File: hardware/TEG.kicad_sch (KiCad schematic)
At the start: 30 parts, among them J1 TEG_IN, J2 FAN_4PIN, J3 TEST_LOAD, Q1 AO3400A, U1 BQ25504RGTT, U2 MT3608

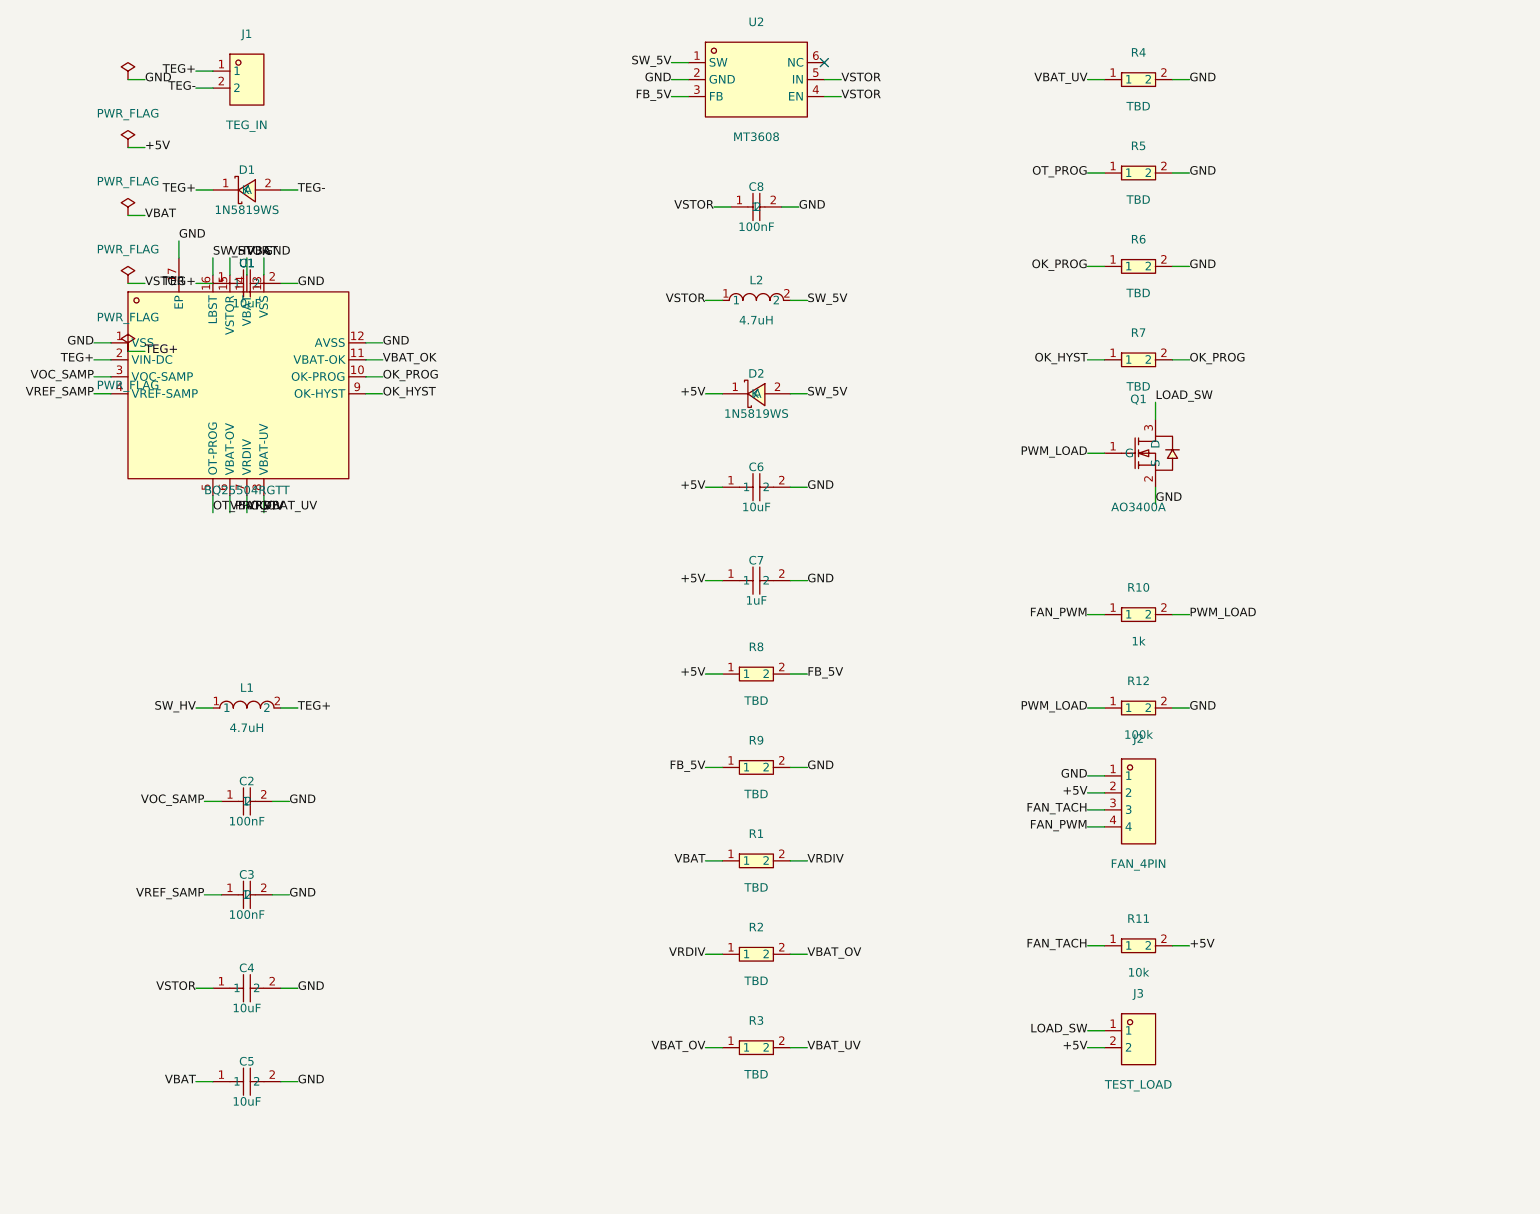
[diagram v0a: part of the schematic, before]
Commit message: Add MPPT sampling network; switch storage to supercapacitor
The BQ25504 has MPPT built in, but the draft was missing its sampling
network. Fixed:

- Add R13/R14 = 10M/10M on VOC_SAMP -> MPP ratio ~50% of Voc
  (TEG matched load; the datasheet's 78% default targets solar)
- CREF/CBYP = 10nF (C1589); drop the 100nF cap that would have slowed
  the high-impedance sampling node
- Fix OV/UV chain order to the datasheet topology and add the missing
  third OK-chain resistor (R15); set threshold values from the datasheet
  worked example (VBAT_OV 3.15V / UV 2.20V / OK 2.44V / HYST 2.80V)
- R5 = 0R ties OT_PROG to GND (65C charge cutoff)
- L1/L2 corrected to the datasheet-recommended 22uH

Storage = supercapacitor 0.22-0.47F/5.5V instead of a battery: safer in a
thermal device (no fire/cold-plating risk), simpler, matches the fan's
burst load. Trade-off noted: measure leakage vs harvest current.

32 parts / 85 pins. ERC: 1 intentional warning; board DRC: 0 violations.
BOM rev B; several high-ohm 1% resistors, the 22uH inductor and the
supercap still need JLCPCB part numbers (all extended / hand-solder).

Co-authored-by: Copilot <223556219+Copilot@users.noreply.github.com>
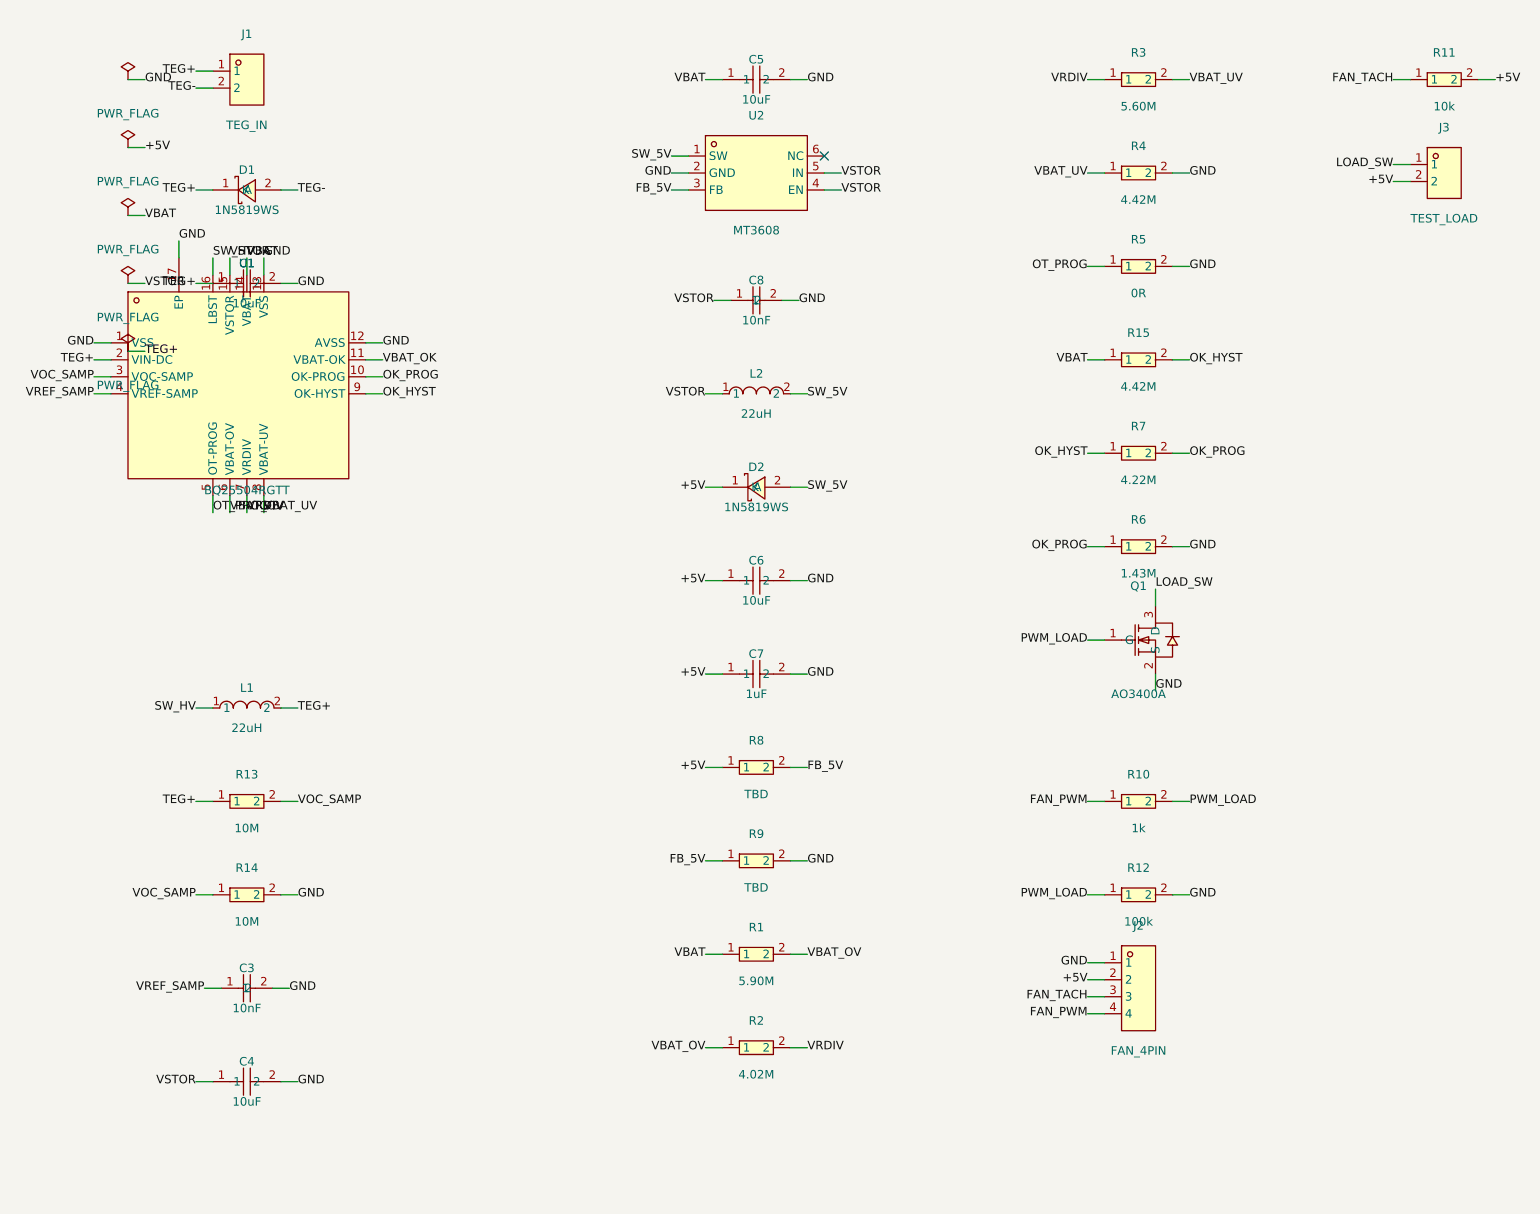
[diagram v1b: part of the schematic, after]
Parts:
- removed C2, C3, C8: 100nF, TEG:C0603, symbol TEG:CL10B104KA8NNNC
- removed R5: TBD, TEG:R0603, symbol TEG:0603WAF1003T5E
- added C3, C8: 10nF, TEG:C0603, symbol TEG:CL10B103KB8NNNC
- added R13, R14: 10M, TEG:R0603, symbol TEG:0603WAF1002T5E
- added R15: 4.42M, TEG:R0603, symbol TEG:0603WAF1003T5E
- added R5: 0R, TEG:R0603, symbol TEG:0603WAF1002T5E
- L1, L2: value 4.7uH -> 22uH; LCSC Part C5832360 -> TBD
- R1: value TBD -> 5.90M
- R2: value TBD -> 4.02M
- R3: value TBD -> 5.60M
- R4: value TBD -> 4.42M
- R6: value TBD -> 1.43M
- R7: value TBD -> 4.22M
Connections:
- net GND: now also C3.2, C8.2, R14.2, R5.2
- net OK_HYST: now also R15.2
- net OT_PROG: now also R5.1
- net TEG+: now also R13.1
- net VBAT: now also R15.1
- net VBAT_OV: now also R1.2, R2.1; no longer R2.2, R3.1
- net VOC_SAMP: now also R13.2, R14.1
- net VRDIV: now also R2.2, R3.1; no longer R1.2, R2.1
- net VREF_SAMP: now also C3.1
- net VSTOR: now also C8.1

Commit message: Set R13/R14 to a real 10M 1% part (C114606); record sourcing reality
Supercaps are not stocked by JLCPCB -> hand-solder. The odd threshold
resistors are standard E96 values but JLCPCB's public search API was
degraded and could not resolve them; note that for the buyer.

Co-authored-by: Copilot <223556219+Copilot@users.noreply.github.com>
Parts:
- R13, R14: LCSC Part TBD -> C114606
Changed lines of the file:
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@@
 		(property "Footprint" "TEG:R0603" (at 0 0 0) (effects (font (size 1.27 1.27)) hide))
 		(property "Datasheet" "~" (at 0 0 0) (effects (font (size 1.27 1.27)) hide))
-		(property "LCSC Part" "TBD" (at 0 0 0) (effects (font (size 1.27 1.27)) hide))
+		(property "LCSC Part" "C114606" (at 0 0 0) (effects (font (size 1.27 1.27)) hide))
 		(pin "2")
 		(pin "1")
@@
 		(property "Footprint" "TEG:R0603" (at 0 0 0) (effects (font (size 1.27 1.27)) hide))
 		(property "Datasheet" "~" (at 0 0 0) (effects (font (size 1.27 1.27)) hide))
-		(property "LCSC Part" "TBD" (at 0 0 0) (effects (font (size 1.27 1.27)) hide))
+		(property "LCSC Part" "C114606" (at 0 0 0) (effects (font (size 1.27 1.27)) hide))
 		(pin "2")
 		(pin "1")

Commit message: Source every part from the JLCPCB catalogue; document the storage decision
jlc-client's search index degraded to returning the same high-stock list
for every query, so add scripts/jlc_lookup.py which queries JLCPCB's own
parts API and reports id + library type + stock.

All 31 machine-placed parts now verified in the catalogue:
- 22uH inductor -> C82401 (SWPA4020S220MT, 4x4mm, 1.05A)
- odd E96 threshold resistors -> C2076902/C137708/C23190/C166806/
  C166807/C166898 (all in stock)
- MT3608 divider computed: 73.2k/10k -> 5.0V (C2933257/C25804)
- R10 -> 1k base part C21190
Flag: BQ25504RGTT (C157471) is low stock (7); C2876746 is the same part.

Confirmed via JLCPCB's API that supercapacitors and batteries are not
stocked at all (0 results), so BOM.md now lays out four storage options
(hand-solder supercap / plug-in header / coin-cell holder / electrolytic)
with stored energy and effort for each.

Normalise pin electrical types in the symbol library (not just at embed
time) and embed library text verbatim, removing the power-pin ERC errors.

ERC: 1 intentional + 2 cosmetic warnings; board DRC: 0 violations.

Co-authored-by: Copilot <223556219+Copilot@users.noreply.github.com>
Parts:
- removed L1, L2: 22uH, TEG:IND-SMD_L2.5-W2.0-VLS252012CX-150M, symbol TEG:FTC252010S4R7MBCA
- added L1, L2: 22uH, TEG:IND-SMD_L4.0-W4.0, symbol TEG:SWPA4020S220MT
- R1: LCSC Part TBD -> C2076902
- R10: LCSC Part TBD -> C21190
- R15, R4: LCSC Part TBD -> C166806
- R2: LCSC Part TBD -> C137708
- R3: LCSC Part TBD -> C23190
- R6: LCSC Part TBD -> C166898
- R7: LCSC Part TBD -> C166807
- R8: value TBD -> 73.2k; LCSC Part TBD -> C2933257
- R9: value TBD -> 10k; LCSC Part TBD -> C25804
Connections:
- net SW_5V: now also L2.2
- net SW_HV: now also L1.1
- net TEG+: now also L1.2
- net VSTOR: now also L2.1
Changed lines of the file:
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@@
 	)
 	(symbol
-		(lib_id "TEG:FTC252010S4R7MBCA")
+		(lib_id "TEG:SWPA4020S220MT")
 		(at 30.48 124.46 0)
 		(unit 1)
@@
 		(property "Reference" "L1" (at 30.48 121.46 0) (effects (font (size 1.27 1.27))))
 		(property "Value" "22uH" (at 30.48 127.46 0) (effects (font (size 1.27 1.27))))
-		(property "Footprint" "TEG:IND-SMD_L2.5-W2.0-VLS252012CX-150M" (at 0 0 0) (effects (font (size 1.27 1.27)) hide))
-		(property "Datasheet" "~" (at 0 0 0) (effects (font (size 1.27 1.27)) hide))
-		(property "LCSC Part" "TBD" (at 0 0 0) (effects (font (size 1.27 1.27)) hide))
+		(property "Footprint" "TEG:IND-SMD_L4.0-W4.0" (at 0 0 0) (effects (font (size 1.27 1.27)) hide))
+		(property "Datasheet" "~" (at 0 0 0) (effects (font (size 1.27 1.27)) hide))
+		(property "LCSC Part" "C82401" (at 0 0 0) (effects (font (size 1.27 1.27)) hide))
 		(pin "2")
 		(pin "1")
@@
 	)
 	(symbol
-		(lib_id "TEG:FTC252010S4R7MBCA")
+		(lib_id "TEG:SWPA4020S220MT")
 		(at 106.68 77.47 0)
 		(unit 1)
@@
 		(property "Reference" "L2" (at 106.68 74.47 0) (effects (font (size 1.27 1.27))))
 		(property "Value" "22uH" (at 106.68 80.47 0) (effects (font (size 1.27 1.27))))
-		(property "Footprint" "TEG:IND-SMD_L2.5-W2.0-VLS252012CX-150M" (at 0 0 0) (effects (font (size 1.27 1.27)) hide))
-		(property "Datasheet" "~" (at 0 0 0) (effects (font (size 1.27 1.27)) hide))
-		(property "LCSC Part" "TBD" (at 0 0 0) (effects (font (size 1.27 1.27)) hide))
+		(property "Footprint" "TEG:IND-SMD_L4.0-W4.0" (at 0 0 0) (effects (font (size 1.27 1.27)) hide))
+		(property "Datasheet" "~" (at 0 0 0) (effects (font (size 1.27 1.27)) hide))
+		(property "LCSC Part" "C82401" (at 0 0 0) (effects (font (size 1.27 1.27)) hide))
 		(pin "2")
 		(pin "1")
@@
 		(exclude_from_sim no) (in_bom yes) (on_board yes) (dnp no) (fields_autoplaced yes)
 		(property "Reference" "R8" (at 106.68 129.33 0) (effects (font (size 1.27 1.27))))
-		(property "Value" "TBD" (at 106.68 137.37 0) (effects (font (size 1.27 1.27))))
-		(property "Footprint" "TEG:R0603" (at 0 0 0) (effects (font (size 1.27 1.27)) hide))
-		(property "Datasheet" "~" (at 0 0 0) (effects (font (size 1.27 1.27)) hide))
-		(property "LCSC Part" "TBD" (at 0 0 0) (effects (font (size 1.27 1.27)) hide))
+		(property "Value" "73.2k" (at 106.68 137.37 0) (effects (font (size 1.27 1.27))))
+		(property "Footprint" "TEG:R0603" (at 0 0 0) (effects (font (size 1.27 1.27)) hide))
+		(property "Datasheet" "~" (at 0 0 0) (effects (font (size 1.27 1.27)) hide))
+		(property "LCSC Part" "C2933257" (at 0 0 0) (effects (font (size 1.27 1.27)) hide))
 		(pin "2")
 		(pin "1")
@@
 		(exclude_from_sim no) (in_bom yes) (on_board yes) (dnp no) (fields_autoplaced yes)
 		(property "Reference" "R9" (at 106.68 143.3 0) (effects (font (size 1.27 1.27))))
-		(property "Value" "TBD" (at 106.68 151.34 0) (effects (font (size 1.27 1.27))))
-		(property "Footprint" "TEG:R0603" (at 0 0 0) (effects (font (size 1.27 1.27)) hide))
-		(property "Datasheet" "~" (at 0 0 0) (effects (font (size 1.27 1.27)) hide))
-		(property "LCSC Part" "TBD" (at 0 0 0) (effects (font (size 1.27 1.27)) hide))
+		(property "Value" "10k" (at 106.68 151.34 0) (effects (font (size 1.27 1.27))))
+		(property "Footprint" "TEG:R0603" (at 0 0 0) (effects (font (size 1.27 1.27)) hide))
+		(property "Datasheet" "~" (at 0 0 0) (effects (font (size 1.27 1.27)) hide))
+		(property "LCSC Part" "C25804" (at 0 0 0) (effects (font (size 1.27 1.27)) hide))
 		(pin "2")
 		(pin "1")
@@
 		(property "Footprint" "TEG:R0603" (at 0 0 0) (effects (font (size 1.27 1.27)) hide))
 		(property "Datasheet" "~" (at 0 0 0) (effects (font (size 1.27 1.27)) hide))
-		(property "LCSC Part" "TBD" (at 0 0 0) (effects (font (size 1.27 1.27)) hide))
+		(property "LCSC Part" "C2076902" (at 0 0 0) (effects (font (size 1.27 1.27)) hide))
 		(pin "2")
 		(pin "1")
@@
 		(property "Footprint" "TEG:R0603" (at 0 0 0) (effects (font (size 1.27 1.27)) hide))
 		(property "Datasheet" "~" (at 0 0 0) (effects (font (size 1.27 1.27)) hide))
-		(property "LCSC Part" "TBD" (at 0 0 0) (effects (font (size 1.27 1.27)) hide))
+		(property "LCSC Part" "C137708" (at 0 0 0) (effects (font (size 1.27 1.27)) hide))
 		(pin "2")
 		(pin "1")
@@
 		(property "Footprint" "TEG:R0603" (at 0 0 0) (effects (font (size 1.27 1.27)) hide))
 		(property "Datasheet" "~" (at 0 0 0) (effects (font (size 1.27 1.27)) hide))
-		(property "LCSC Part" "TBD" (at 0 0 0) (effects (font (size 1.27 1.27)) hide))
+		(property "LCSC Part" "C23190" (at 0 0 0) (effects (font (size 1.27 1.27)) hide))
 		(pin "2")
 		(pin "1")
@@
 		(property "Footprint" "TEG:R0603" (at 0 0 0) (effects (font (size 1.27 1.27)) hide))
 		(property "Datasheet" "~" (at 0 0 0) (effects (font (size 1.27 1.27)) hide))
-		(property "LCSC Part" "TBD" (at 0 0 0) (effects (font (size 1.27 1.27)) hide))
+		(property "LCSC Part" "C166806" (at 0 0 0) (effects (font (size 1.27 1.27)) hide))
 		(pin "2")
 		(pin "1")
@@
 		(property "Footprint" "TEG:R0603" (at 0 0 0) (effects (font (size 1.27 1.27)) hide))
 		(property "Datasheet" "~" (at 0 0 0) (effects (font (size 1.27 1.27)) hide))
-		(property "LCSC Part" "TBD" (at 0 0 0) (effects (font (size 1.27 1.27)) hide))
+		(property "LCSC Part" "C166806" (at 0 0 0) (effects (font (size 1.27 1.27)) hide))
 		(pin "2")
 		(pin "1")
@@
 		(property "Footprint" "TEG:R0603" (at 0 0 0) (effects (font (size 1.27 1.27)) hide))
 		(property "Datasheet" "~" (at 0 0 0) (effects (font (size 1.27 1.27)) hide))
-		(property "LCSC Part" "TBD" (at 0 0 0) (effects (font (size 1.27 1.27)) hide))
+		(property "LCSC Part" "C166807" (at 0 0 0) (effects (font (size 1.27 1.27)) hide))
 		(pin "2")
 		(pin "1")
@@
 		(property "Footprint" "TEG:R0603" (at 0 0 0) (effects (font (size 1.27 1.27)) hide))
 		(property "Datasheet" "~" (at 0 0 0) (effects (font (size 1.27 1.27)) hide))
-		(property "LCSC Part" "TBD" (at 0 0 0) (effects (font (size 1.27 1.27)) hide))
+		(property "LCSC Part" "C166898" (at 0 0 0) (effects (font (size 1.27 1.27)) hide))
 		(pin "2")
 		(pin "1")
@@
 		(property "Footprint" "TEG:R0603" (at 0 0 0) (effects (font (size 1.27 1.27)) hide))
 		(property "Datasheet" "~" (at 0 0 0) (effects (font (size 1.27 1.27)) hide))
-		(property "LCSC Part" "TBD" (at 0 0 0) (effects (font (size 1.27 1.27)) hide))
-		(pin "2")
-		(pin "1")
+		(property "LCSC Part" "C21190" (at 0 0 0) (effects (font (size 1.27 1.27)) hide))
+		(pin "2")
+		(pin "1")

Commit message: Storage: option D electrolytic buffer (100% JLCPCB assembled)
The user chose the fully-automated path: no supercap, no battery. Adds
C2 = 1000uF 6.3V SMD electrolytic (C970711) as the VBAT buffer, which is
what the BQ25504 needs to operate (datasheet reference shows >100uF).

Consequences documented rather than glossed over: with ~5mJ stored (vs
~1.2J for a supercap) the fan can only run on live harvest, not from
storage. VBAT_OK is left unconnected with a no-connect marker; the
datasheet confirms it is a low-drive digital output referenced to VSTOR,
so gating the load would need extra parts - deferred.

Also: pin-type normalisation now never clobbers power pins (a previous
pass had turned PWR_FLAG's power_out into passive, which made 4 power
nets report as undriven).

Board = 33 parts. ERC: 3 cosmetic warnings. DRC: 1 cosmetic silkscreen
warning. Remaining: routing.

Co-authored-by: Copilot <223556219+Copilot@users.noreply.github.com>
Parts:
- added C2: 1000uF, TEG:CAP-SMD_BD8.0-L8.3-W8.3-LS9.3-FD-1, symbol TEG:RVT0J102M08101000UF6.3V
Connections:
- net GND: now also C2.2
- net VBAT: now also C2.1
- net VBAT_OK: no longer names the net of U1.11 (VBAT-OK)
- no-connect marks 1 -> 2
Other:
- note added: "DRAFT — nets defined by labels at each pin; no routed wires yet. Storage: 1000uF electrolytic buffer on VBAT (JLCPCB-assembled, polarised - check pin 1). There is no energy store beyond this buffer, so the fan runs only while the TEGs supply power; VBAT_OK is left unconnected (available later for load gating)."
- note removed: "DRAFT — nets defined by labels at each pin; no routed wires yet. TBD: storage element on VBAT (supercap vs Li-ion); programming resistors R1-R9 pending BQ25504/MT3608 datasheet math. External PWM source drives FAN_PWM (fan speed + test-load gate via R10/R12)."
